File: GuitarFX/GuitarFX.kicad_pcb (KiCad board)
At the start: 4 copper layers, 70 x 85 mm, 122 parts, among them IC401 PCM3060PWR, J202 Screw_Terminal_01x02, J301 USB_C_Receptacle_USB2.0, J302 Conn_ARM_SWD_TagConnect_TC2030, J303 Screw_Terminal_01x06, J401 Screw_Terminal_01x02, J402 Screw_Terminal_01x02, SW301 SW_SPDT, U201 NCP718xSN500, U202 NCP1117-3.3_SOT223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

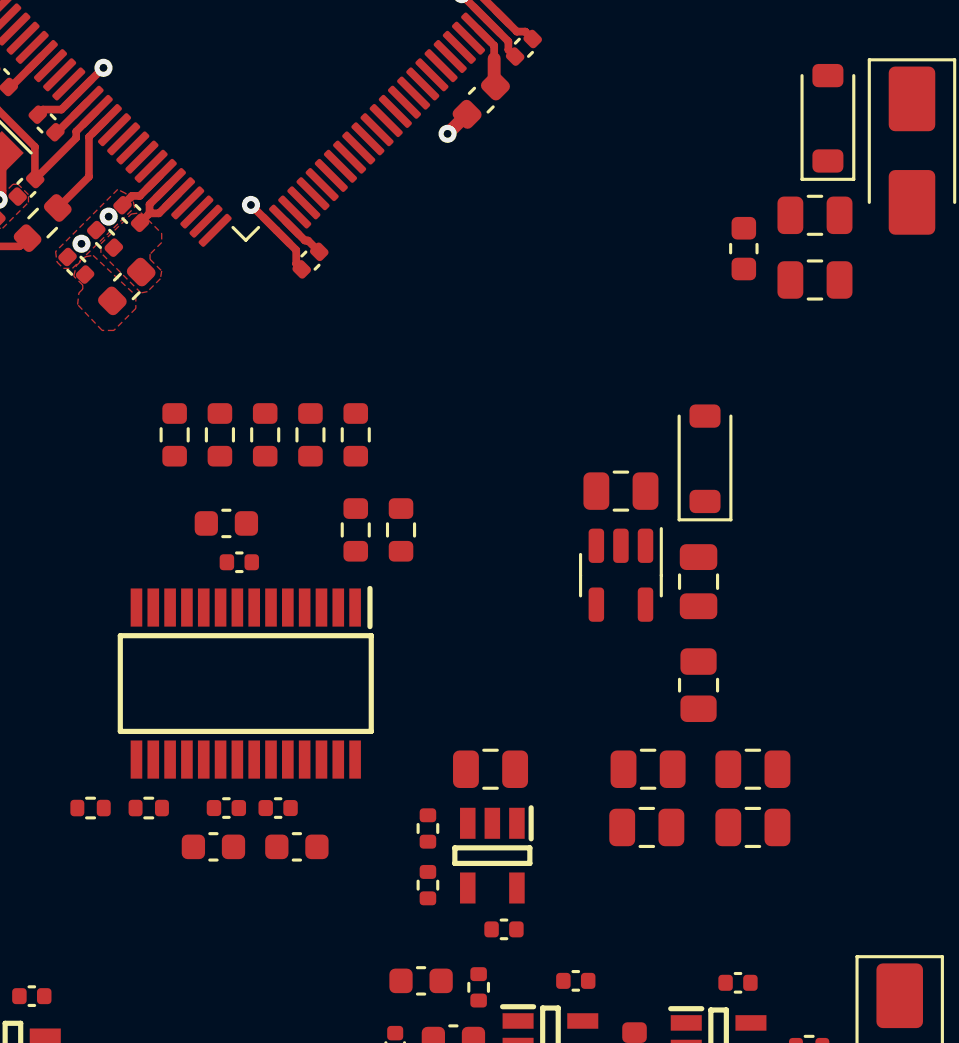
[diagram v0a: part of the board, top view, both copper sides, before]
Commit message: Finished routing for i2s
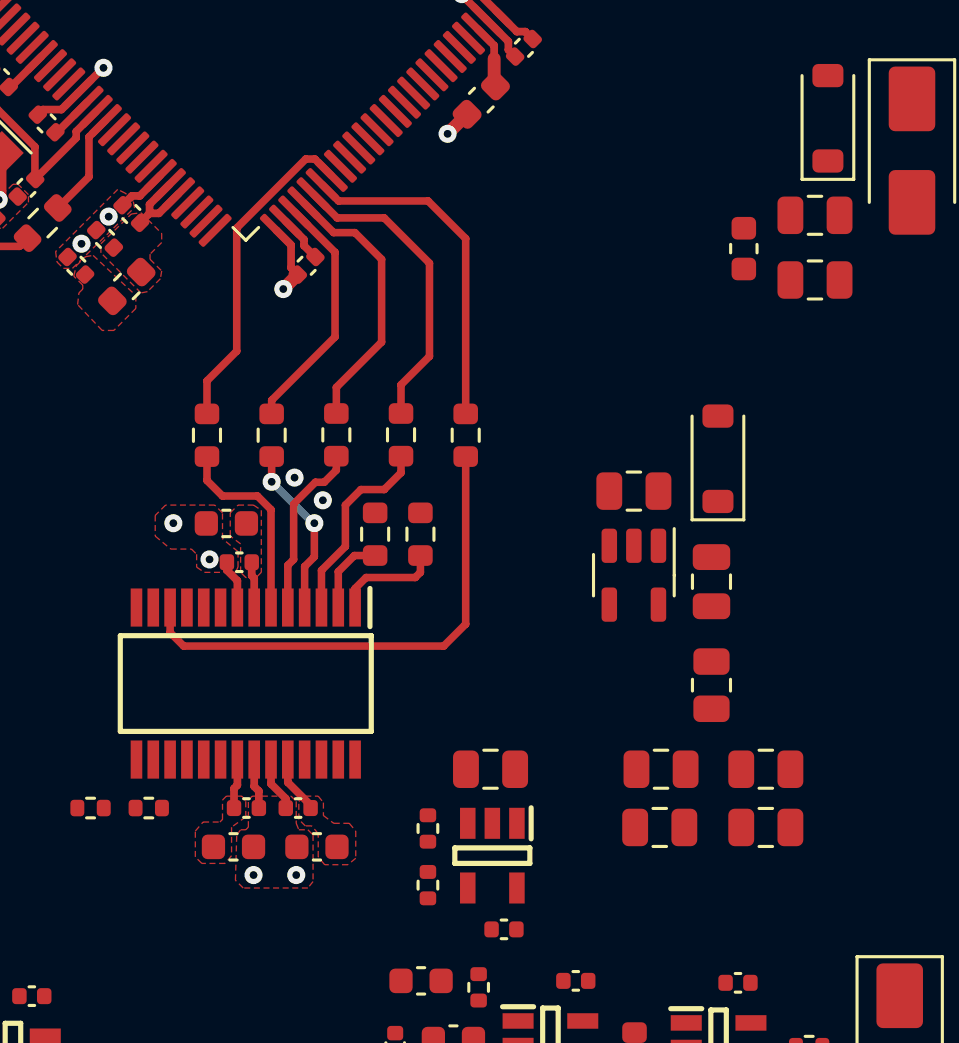
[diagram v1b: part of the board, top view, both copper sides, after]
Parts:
- moved R428 11.3 mm to (153.5, 106.5)
- moved R424 2.75 mm to (148.5, 106.5)
- moved R419 1.75 mm to (151.0, 106.5)
- moved R420 1.50 mm to (146.0, 106.5)
- moved C430 0.78 mm to (147.8, 122.4)
- moved C431 0.78 mm to (147.0, 120.9)
- moved C432 0.78 mm to (144.5, 122.4)
- moved C433 0.78 mm to (145.0, 120.9)
- moved R417 0.77 mm to (151.8, 110.3)
- moved R418 0.77 mm to (150.0, 110.3)
- moved R426 0.50 mm to (143.5, 106.5)
- moved C201 0.50 mm to (165.1, 119.4)
- moved C202 0.50 mm to (165.1, 121.7)
- moved C203 0.50 mm to (161.0, 121.7)
- moved C204 0.50 mm to (161.1, 119.4)
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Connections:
- R419 pad 1: I2S1_SDO -> I2S1_SDI
- R428 pad 1: I2S1_SDI -> I2S1_SDO
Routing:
- net /Codec/CODEC_DIN: track 0.00 -> 19.4 mm
- net I2S1_SDO: track 0.00 -> 13.2 mm
- net I2S1_MCK: track 0.00 -> 12.7 mm
- net I2S1_SDI: track 0.00 -> 11.9 mm
- net I2S1_CK: track 0.00 -> 10.6 mm
- net I2S1_WS: track 0.00 -> 9.46 mm
- net /Codec/CODEC_SCK1: track 0.00 -> 7.69 mm
- net /Codec/CODEC_DOUT: track 0.00 -> 7.65 mm
- net /Codec/CODEC_BCK1: track 0.00 -> 6.83 mm
- net /Codec/CODEC_LRCK1: track 0.00 -> 6.77 mm, vias 0 -> 2
- net GND: track 37.7 -> 43.3 mm, vias 25 -> 31
- net I2C1_SCL: track 0.00 -> 4.17 mm
- net I2C1_SDA: track 0.00 -> 3.07 mm
- net +5VA: track 0.00 -> 2.24 mm
- net /Codec/CODEC_VCOM: track 0.00 -> 1.93 mm
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- added copper zone on F.Cu, net +5VA
- added copper zone on F.Cu, net /Codec/CODEC_VCOM

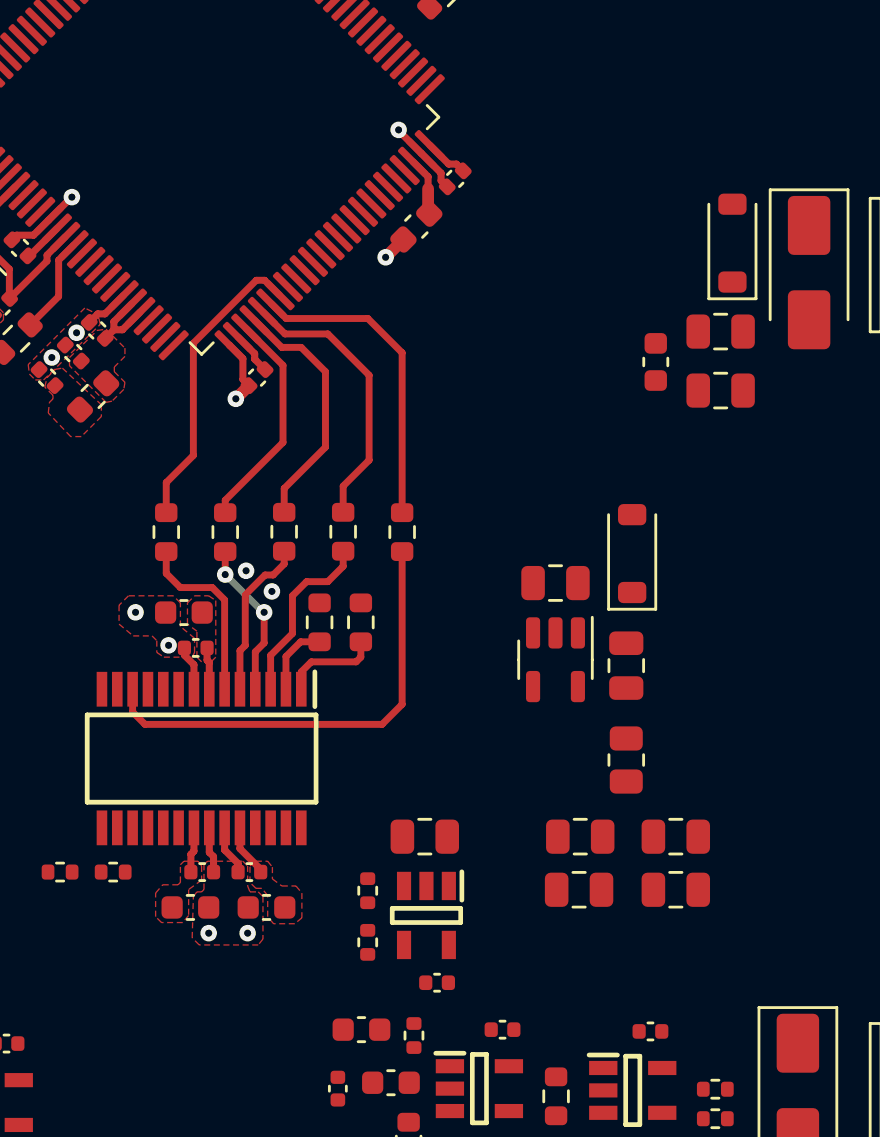
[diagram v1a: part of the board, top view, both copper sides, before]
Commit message: Updated I2C pins for easier routing
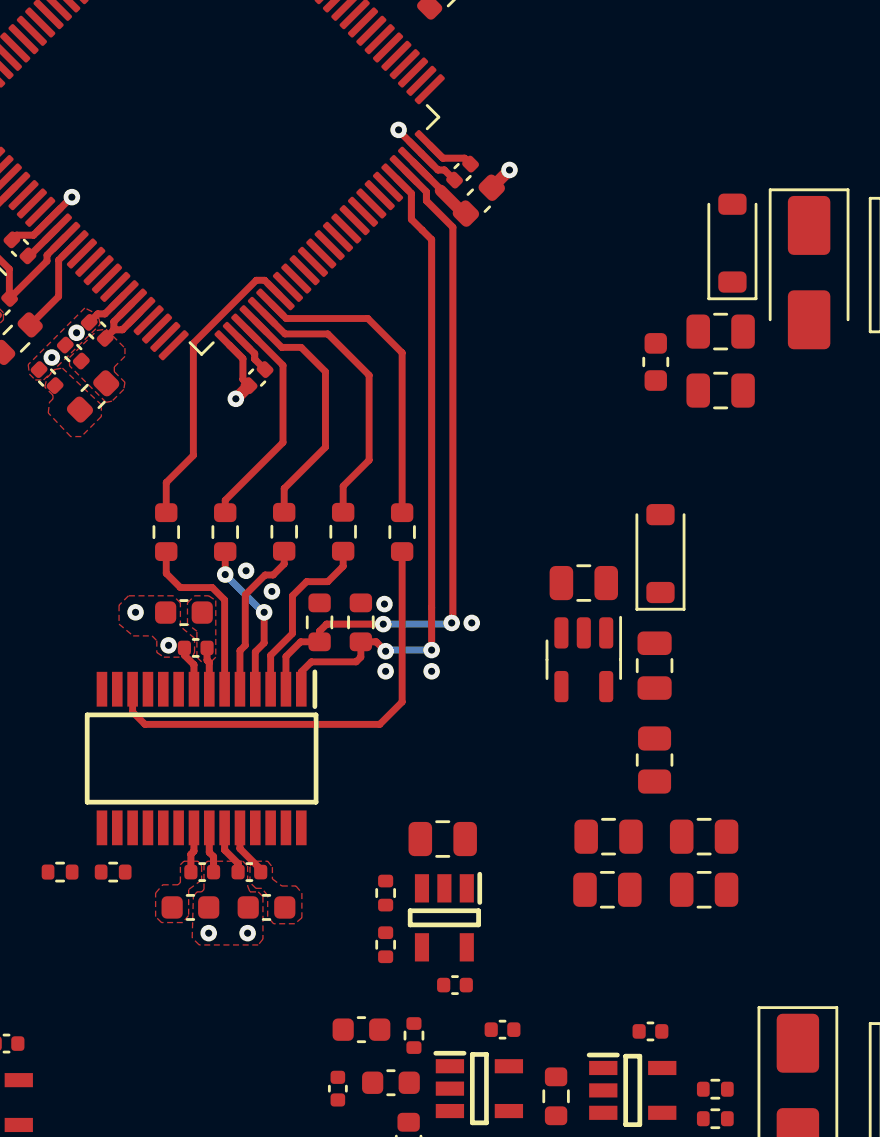
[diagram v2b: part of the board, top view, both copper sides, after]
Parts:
- moved C318 2.87 mm to (156.8, 92.5), turned to 45 degrees
- moved C201 1.20 mm to (166.3, 119.4)
- moved C202 1.20 mm to (166.3, 121.7)
- moved C203 1.20 mm to (162.2, 121.7)
- moved C204 1.20 mm to (162.2, 119.4)
- moved C207 1.20 mm to (161.2, 108.7)
- moved C208 1.20 mm to (164.2, 112.2)
- moved D201 1.20 mm to (164.4, 107.4)
- moved R201 1.20 mm to (164.2, 116.2)
- moved U201 1.20 mm to (161.2, 111.9)
- moved C402 0.77 mm to (155.7, 125.7)
- moved R401 0.77 mm to (152.8, 124.0)
- moved R403 0.77 mm to (152.8, 121.8)
- moved C405 0.77 mm to (155.2, 119.5)
- moved U401 0.77 mm to (155.3, 122.8)
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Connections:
- U302 pad 46: unconnected-(U302-PB10-Pad46) -> I2C1_SCL
- U302 pad 47: unconnected-(U302-PB11-Pad47) -> I2C1_SDA
- U302 pad 92: I2C1_SCL -> unconnected-(U302-PB6-Pad92)
- U302 pad 93: I2C1_SDA -> unconnected-(U302-PB7-Pad93)
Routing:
- net I2C1_SDA: track 3.07 -> 29.3 mm, vias 0 -> 2
- net I2C1_SCL: track 4.17 -> 28.0 mm, vias 0 -> 2
- net /MCU/MCU_VCAP1: track 2.48 -> 4.14 mm
- net GND: vias 31 -> 35

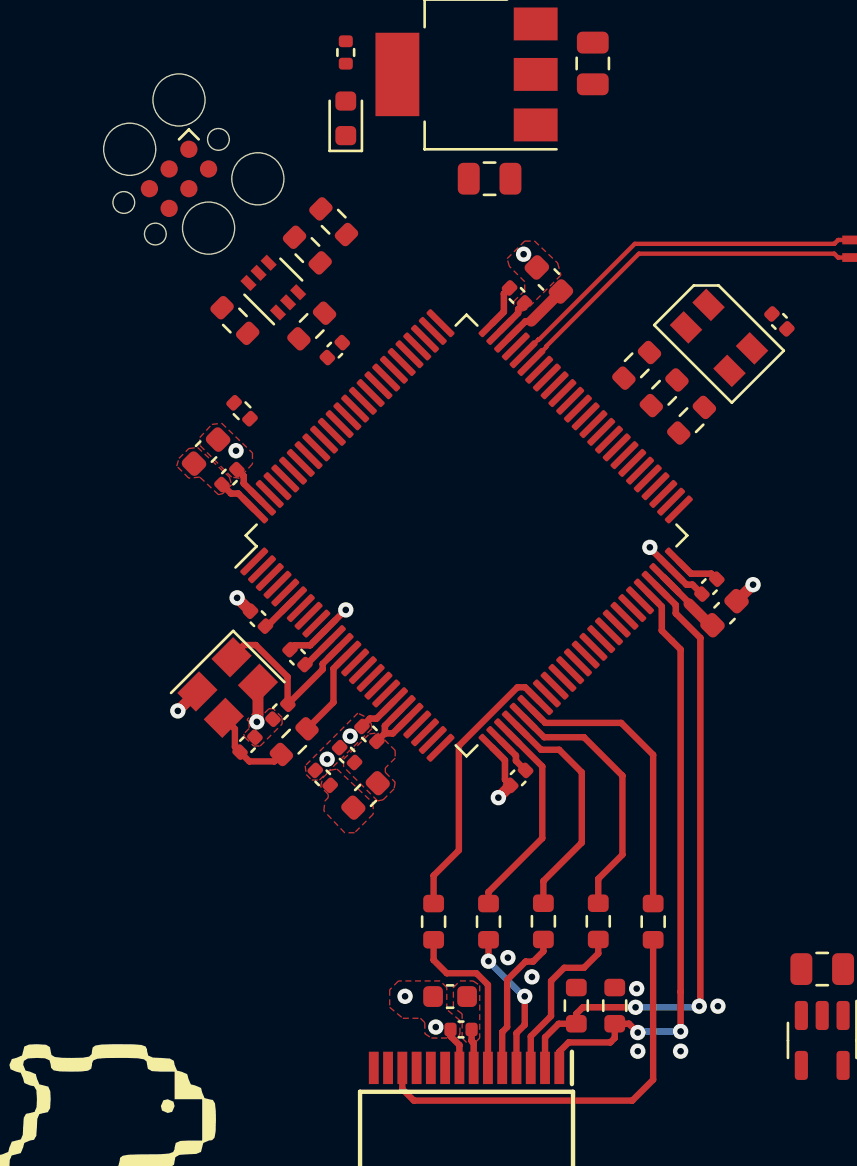
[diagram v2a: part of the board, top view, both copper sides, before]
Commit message: SWD routing done
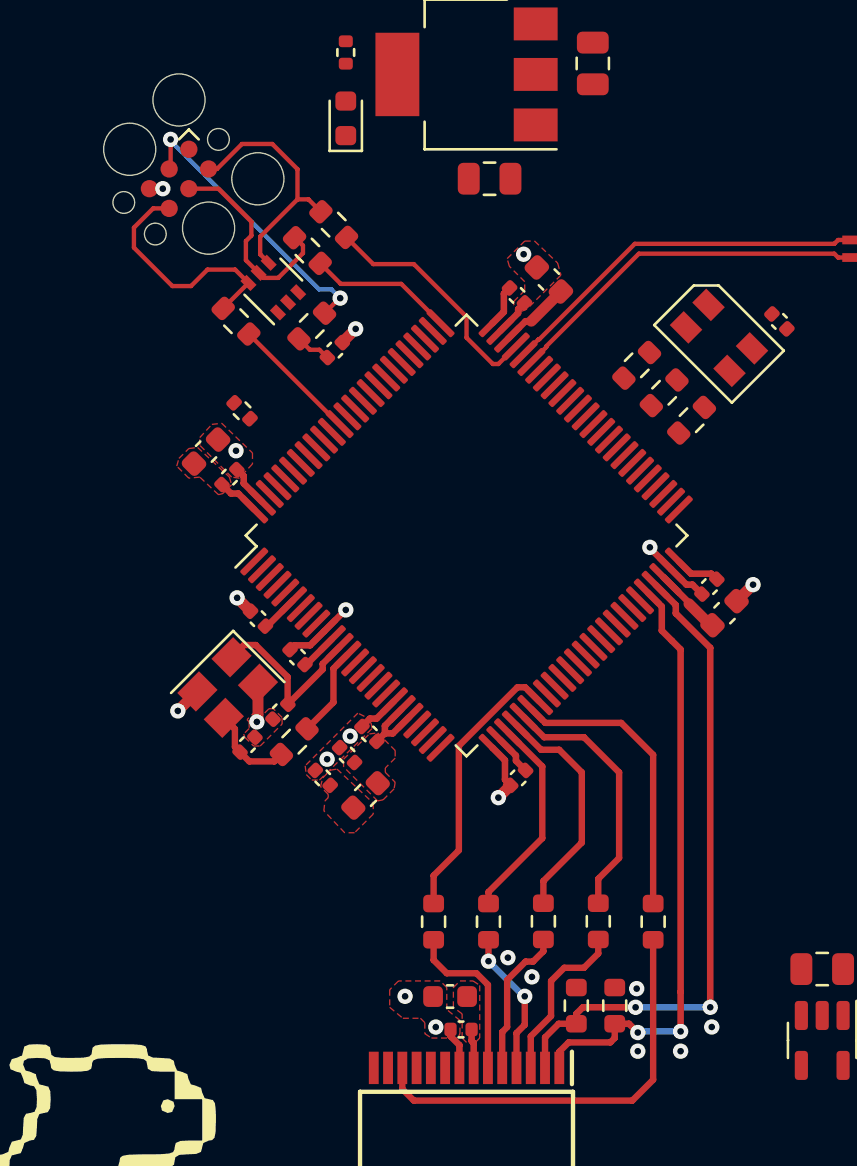
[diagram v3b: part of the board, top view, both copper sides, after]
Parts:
- moved R305 0.13 mm to (138.9, 74.8)
- moved R307 0.06 mm to (134.5, 79.2)
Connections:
- D302 pad 4: /MCU/SWCLK -> /MCU/SWDIO
- D302 pad 5: /MCU/SWDIO -> /MCU/SWCLK
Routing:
- net /MCU/NRST: track 0.00 -> 13.1 mm, vias 0 -> 2
- net /MCU/SWDIO: track 0.00 -> 11.4 mm
- net /MCU/SWO: track 0.00 -> 11.0 mm
- net /MCU/MCU_SWDIO: track 0.00 -> 11.0 mm
- net /MCU/SWCLK: track 0.00 -> 9.63 mm
- net /MCU/MCU_SWCLK: track 0.00 -> 6.61 mm
- net /MCU/MCU_SWO: track 0.00 -> 5.84 mm
- net /MCU/MCU_NRST: track 0.00 -> 1.65 mm
- net GND: track 43.3 -> 44.7 mm, vias 35 -> 37
- net I2C1_SDA: track 29.3 -> 30.0 mm
